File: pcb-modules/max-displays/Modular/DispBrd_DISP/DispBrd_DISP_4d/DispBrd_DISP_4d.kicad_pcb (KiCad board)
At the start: 2 copper layers, 30 x 19.3 mm, 4 parts, among them P5 Disp4b

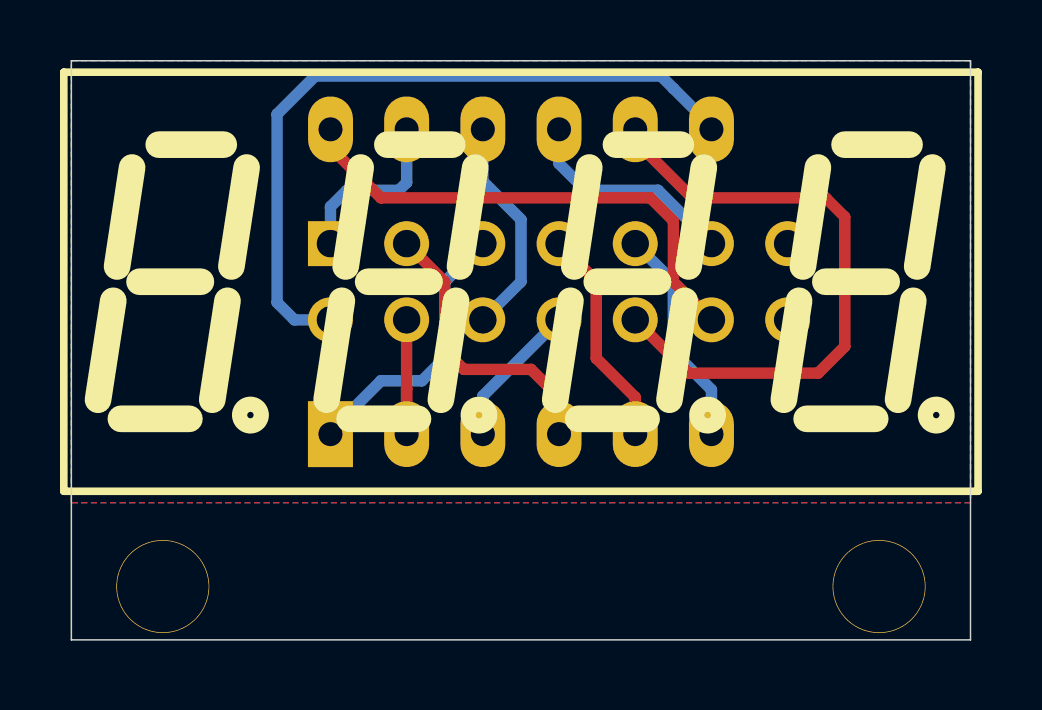
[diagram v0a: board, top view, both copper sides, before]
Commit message: Max Display panels, modular version FIX: Rear connector rotated 180deg on boards [3+2d], [3+3d], [6x1d] All boards: Silkscreen text on rear oriented correctly; board name added; Format update to KiCAD 6.0.6
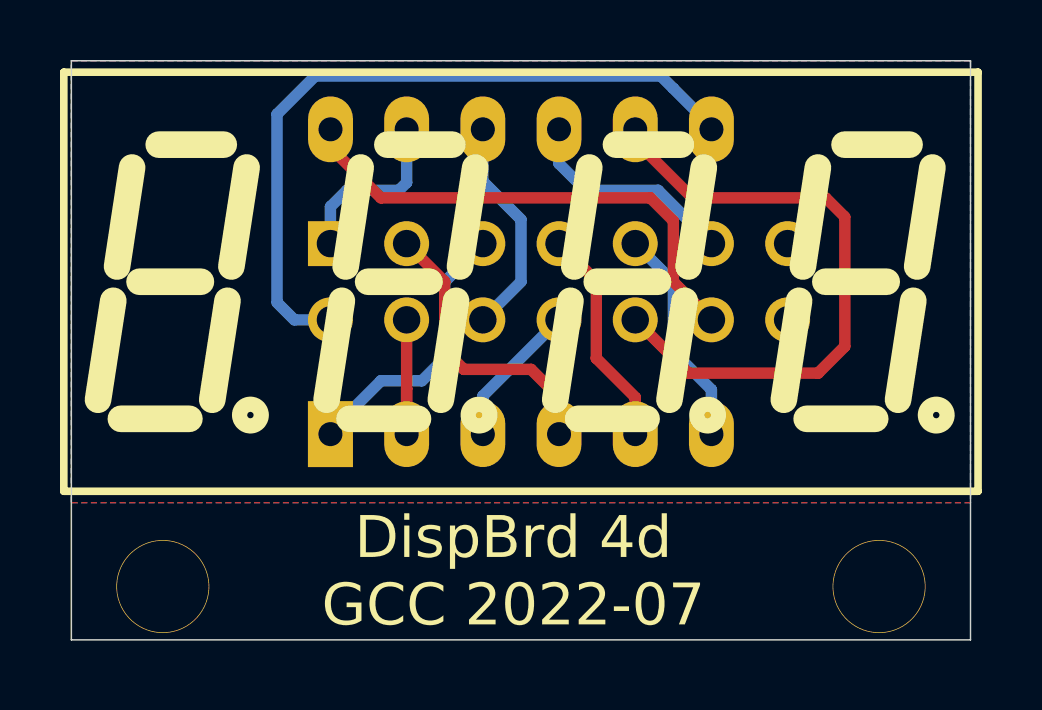
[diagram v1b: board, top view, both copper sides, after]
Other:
- board text added: "DispBrd 4d GCC 2022-07"
- board text added: "K3 K1 G E C A"
- board text added: "K4 K2 dp F D B"
- board text removed: "A C E G K1 K3"
- board text removed: "B D F dp K2 K4"
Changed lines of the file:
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@@
   )
   (gr_rect (start 25.4 22.86) (end 55.372 42.164) (layer "Edge.Cuts") (width 0.05) (fill none))
-  (gr_text "A  C  E  G K1 K3" (at 40.64 27.178 180) (layer "B.SilkS")
+  (gr_text "K3 K1 G  E  C  A" (at 40.64 27.178) (layer "B.SilkS")
     (effects (font (size 1.27 1.016) (thickness 0.2032)) (justify mirror))
   )
-  (gr_text "B  D  F dp K2 K4" (at 40.64 33.274 180) (layer "B.SilkS")
+  (gr_text "K4 K2 dp F  D  B" (at 40.64 33.274) (layer "B.SilkS")
     (effects (font (size 1.27 1.016) (thickness 0.2032)) (justify mirror))
   )
+  (gr_text "DispBrd 4d\nGCC 2022-07" (at 40.132 39.878) (layer "B.SilkS")
+    (effects (font (size 1.397 1.397) (thickness 0.254)) (justify mirror))
+  )
+  (gr_text "DispBrd 4d\nGCC 2022-07" (at 40.132 39.878) (layer "F.SilkS")
+    (effects (font (size 1.397 1.397) (thickness 0.254)))
+  )
   (segment (start 36.322 27.178) (end 36.576 26.924) (width 0.381) (layer "B.Cu") (net 1))
